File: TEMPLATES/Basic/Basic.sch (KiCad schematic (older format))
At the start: 2 parts, among them U1 CpE-3004_LP2985_LDO_1v8

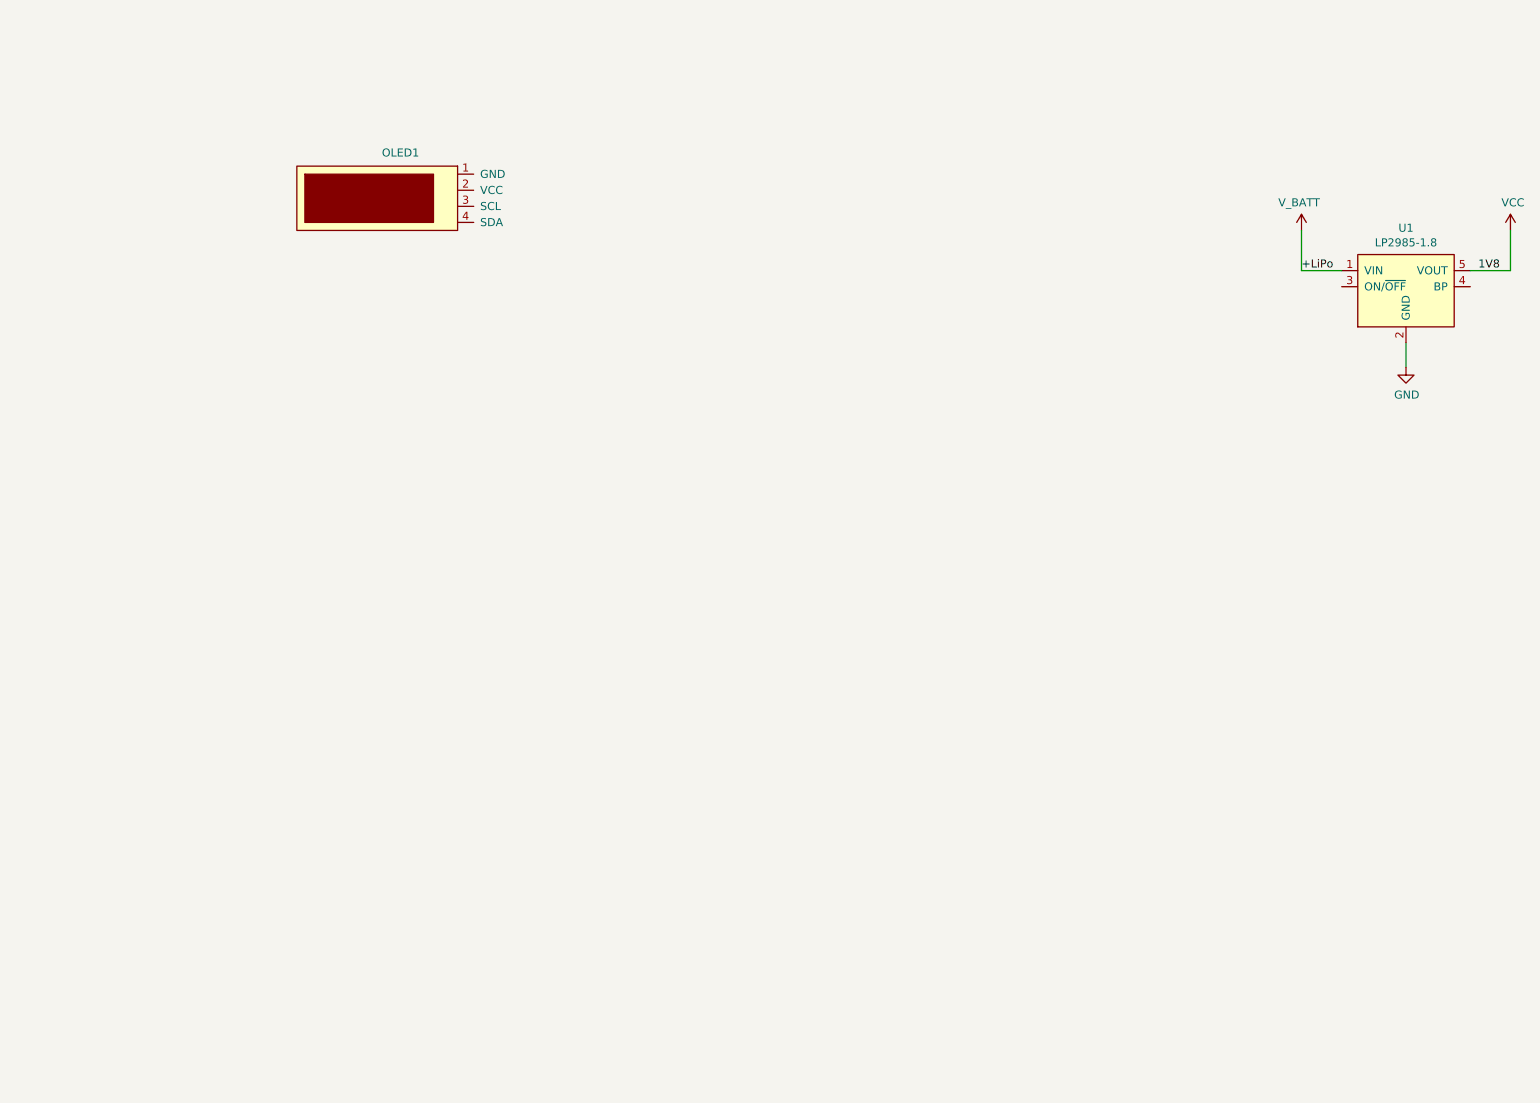
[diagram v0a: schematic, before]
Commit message: Added PCIe-x4 template
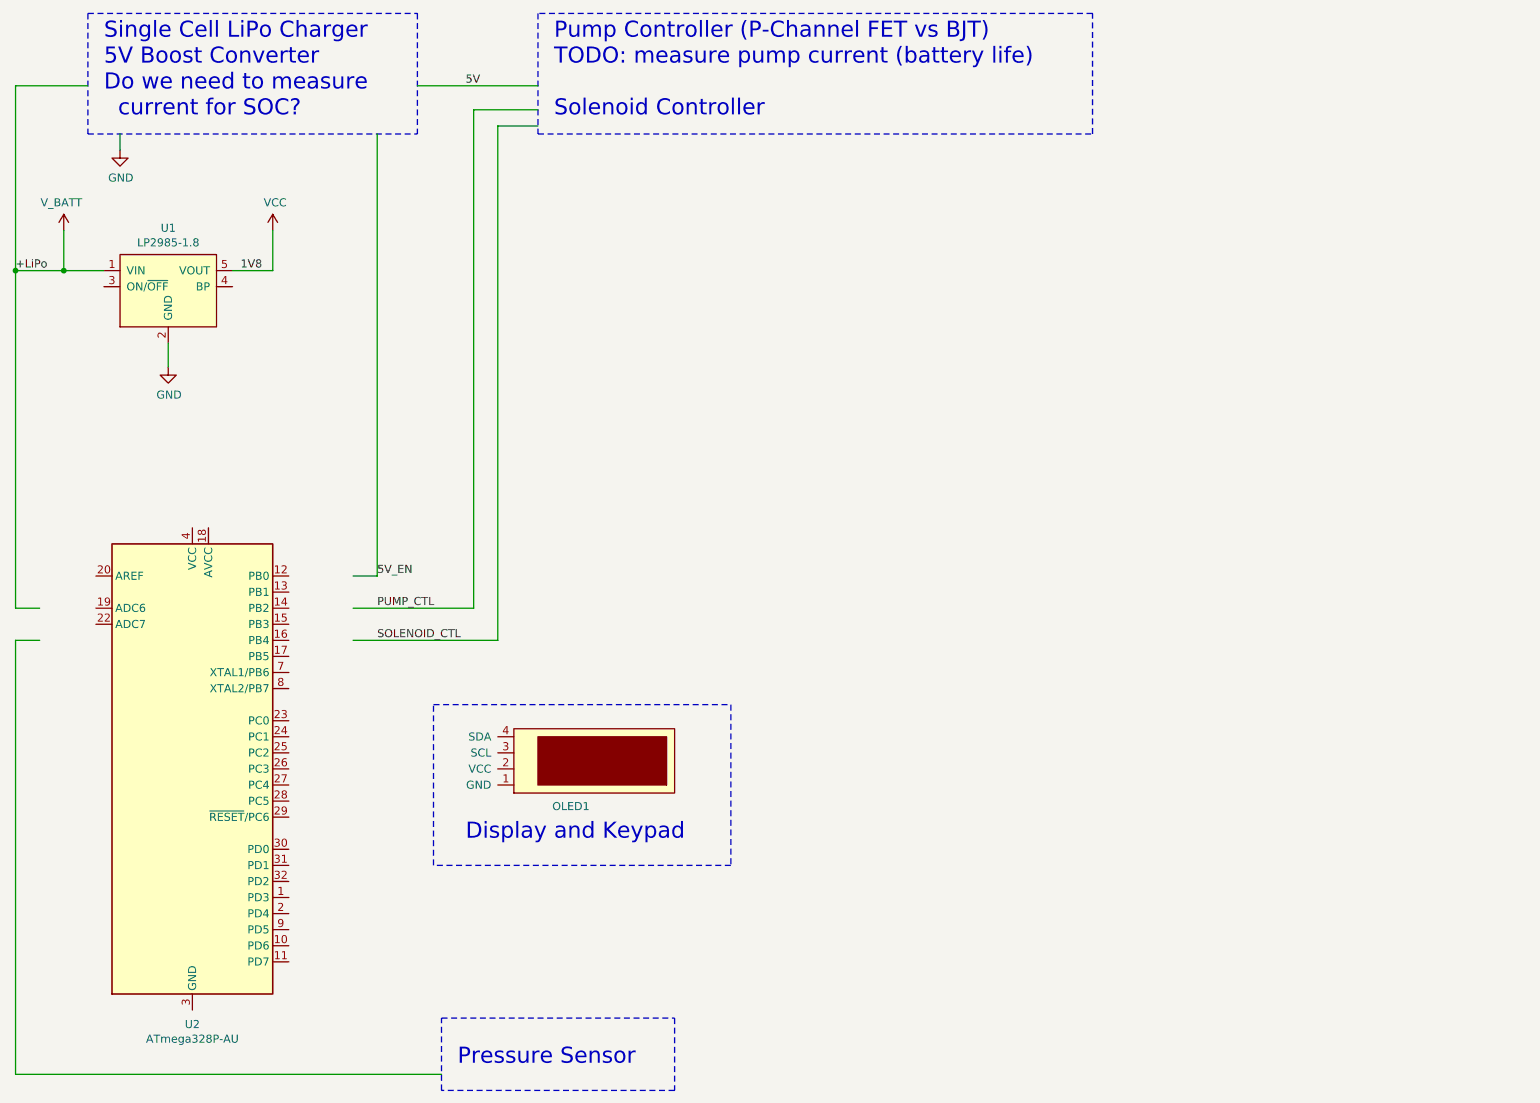
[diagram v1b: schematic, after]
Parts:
- added U2: ATmega328P-AU, Package_QFP:TQFP-32_7x7mm_P0.8mm, symbol MCU_Microchip_ATmega:ATmega328P-AU
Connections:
- net labels added: 5V, 5V_EN, PUMP_CTL, SOLENOID_CTL
- wire segments 5 -> 23
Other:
- note added: "Display and Keypad\n"
- note added: "Pressure Sensor\n"
- note added: "Pump Controller (P-Channel FET vs BJT)\nTODO: measure pump current (battery life)\n\nSolenoid Controller\n"
- note added: "Single Cell LiPo Charger\n5V Boost Converter\nDo we need to measure\n current for SOC?"
- moved on the sheet: OLED1, U1
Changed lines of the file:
@@
 EELAYER 30 0
 EELAYER END
-$Descr A4 11693 8268
+$Descr USLetter 11000 8500
 encoding utf-8
 Sheet 1 1
-Title ""
-Date ""
-Rev ""
+Title "Perfusion Pump Controller"
+Date "2021-12-02"
+Rev "0.1"
 Comp ""
 Comment1 ""
@@
 L CpE_Power:GND #PWR0101
 U 1 1 619BDDDF
-P 9550 2950
-F 0 "#PWR0101" H 9550 2700 50  0001 C CNN
-F 1 "GND" H 9555 2777 50  0000 C CNN
-F 2 "" H 9550 2950 50  0001 C CNN
-F 3 "" H 9550 2950 50  0001 C CNN
-F 4 "NA" H 9550 2950 50  0001 C CNN "CpE_PN"
-	1    9550 2950
+P 1850 2950
+F 0 "#PWR0101" H 1850 2700 50  0001 C CNN
+F 1 "GND" H 1855 2777 50  0000 C CNN
+F 2 "" H 1850 2950 50  0001 C CNN
+F 3 "" H 1850 2950 50  0001 C CNN
+F 4 "NA" H 1850 2950 50  0001 C CNN "CpE_PN"
+	1    1850 2950
 	1    0    0    -1
 $EndComp
@@
 L CpE_Integrated_Circuits:CpE-3004_LP2985_LDO_1v8 U1
 U 1 1 619BE36A
-P 9550 2450
-F 0 "U1" H 9550 2815 50  0000 C CNN
-F 1 "CpE-3004_LP2985_LDO_1v8" H 9550 2900 50  0001 C CNN
-F 2 "CpE_Integrated_Circuits:CpE-3004_LP2985_LDO_1v8" H 9550 3000 50  0001 C CNN
-F 3 "https://www.ti.com/lit/ds/symlink/lp2985.pdf?HQS=dis-dk-null-digikeymode-dsf-pf-null-wwe&ts=1637600572863" H 9550 2450 50  0001 C CNN
-F 4 "3004" H 9550 2800 50  0001 C CNN "CpE_PN"
-F 5 "LP2985-1.8" H 9550 2724 50  0000 C CNN "Val"
-	1    9550 2450
+P 1850 2450
+F 0 "U1" H 1850 2815 50  0000 C CNN
+F 1 "CpE-3004_LP2985_LDO_1v8" H 1850 2900 50  0001 C CNN
+F 2 "CpE_Integrated_Circuits:CpE-3004_LP2985_LDO_1v8" H 1850 3000 50  0001 C CNN
+F 3 "https://www.ti.com/lit/ds/symlink/lp2985.pdf?HQS=dis-dk-null-digikeymode-dsf-pf-null-wwe&ts=1637600572863" H 1850 2450 50  0001 C CNN
+F 4 "3004" H 1850 2800 50  0001 C CNN "CpE_PN"
+F 5 "LP2985-1.8" H 1850 2724 50  0000 C CNN "Val"
+	1    1850 2450
 	1    0    0    -1
 $EndComp
@@
 L CpE_Power:VCC #PWR0102
 U 1 1 619BEDF8
-P 10200 2100
-F 0 "#PWR0102" H 10200 1950 50  0001 C CNN
-F 1 "VCC" H 10215 2273 50  0000 C CNN
-F 2 "" H 10200 2100 50  0001 C CNN
-F 3 "" H 10200 2100 50  0001 C CNN
-F 4 "NA" H 10200 2100 50  0001 C CNN "CpE_PN"
-	1    10200 2100
+P 2500 2100
+F 0 "#PWR0102" H 2500 1950 50  0001 C CNN
+F 1 "VCC" H 2515 2273 50  0000 C CNN
+F 2 "" H 2500 2100 50  0001 C CNN
+F 3 "" H 2500 2100 50  0001 C CNN
+F 4 "NA" H 2500 2100 50  0001 C CNN "CpE_PN"
+	1    2500 2100
 	1    0    0    -1
 $EndComp
-Text Label 10000 2350 0    50   ~ 0
+Text Label 2300 2350 0    50   ~ 0
 1V8
 Wire Wire Line
-	9950 2350 10200 2350
+	2250 2350 2500 2350
 Wire Wire Line
-	10200 2350 10200 2100
+	2500 2350 2500 2100
 Wire Wire Line
-	9550 2950 9550 2800
+	1850 2950 1850 2800
 $Comp
 L CpE_Power:V_BATT #PWR1
 U 1 1 619C0899
-P 8900 2100
-F 0 "#PWR1" H 8900 2100 50  0001 C CNN
-F 1 "V_BATT" H 8885 2273 50  0000 C CNN
-F 2 "" H 8900 2100 50  0001 C CNN
-F 3 "" H 8900 2100 50  0001 C CNN
-	1    8900 2100
+P 1200 2100
+F 0 "#PWR1" H 1200 2100 50  0001 C CNN
+F 1 "V_BATT" H 1185 2273 50  0000 C CNN
+F 2 "" H 1200 2100 50  0001 C CNN
+F 3 "" H 1200 2100 50  0001 C CNN
+	1    1200 2100
 	1    0    0    -1
 $EndComp
 Wire Wire Line
-	8900 2100 8900 2350
+	1200 2100 1200 2350
 Wire Wire Line
-	8900 2350 9150 2350
-Text Label 8900 2350 0    50   ~ 0
+	1200 2350 1450 2350
+Text Label 900  2350 0    50   ~ 0
 +LiPo
 $Comp
 L CpE_Opto_Electronics:CpE-3005_OLED_I2C_128x32 OLED1
 U 1 1 619C1A31
-P 3150 1900
-F 0 "OLED1" H 3295 2183 50  0000 C CNN
-F 1 "CpE-3005_OLED_I2C_128x32" H 3150 2250 50  0001 C CNN
-F 2 "CpE_Opto_Electronics:3005_OLED_I2C_128x32" H 3150 1900 50  0001 C CNN
-F 3 "https://www.amazon.com/Pieces-Display-Module-SSD1306-3-3V-5V/dp/B08L7QW7SR/ref=sr_1_1?keywords=B08L7QW7SR&qid=1637605536&sr=8-1" H 3150 1900 50  0001 C CNN
-F 4 "3005" H 3150 2150 50  0001 C CNN "CpE_PN"
-F 5 "" H 3150 1900 50  0000 C CNN "Val"
-	1    3150 1900
+P 4500 5400
+F 0 "OLED1" H 4645 5683 50  0000 C CNN
+F 1 "CpE-3005_OLED_I2C_128x32" H 4500 5750 50  0001 C CNN
+F 2 "CpE_Opto_Electronics:3005_OLED_I2C_128x32" H 4500 5400 50  0001 C CNN
+F 3 "https://www.amazon.com/Pieces-Display-Module-SSD1306-3-3V-5V/dp/B08L7QW7SR/ref=sr_1_1?keywords=B08L7QW7SR&qid=1637605536&sr=8-1" H 4500 5400 50  0001 C CNN
+F 4 "3005" H 4500 5650 50  0001 C CNN "CpE_PN"
+F 5 "" H 4500 5400 50  0000 C CNN "Val"
+	1    4500 5400
+	-1   0    0    1
+$EndComp
+$Comp
+L MCU_Microchip_ATmega:ATmega328P-AU U2
+U 1 1 61A9199E
+P 2000 5450
+F 0 "U2" H 2000 3861 50  0000 C CNN
+F 1 "ATmega328P-AU" H 2000 3770 50  0000 C CNN
+F 2 "Package_QFP:TQFP-32_7x7mm_P0.8mm" H 2000 5450 50  0001 C CIN
+F 3 "http://ww1.microchip.com/downloads/en/DeviceDoc/ATmega328_P%20AVR%20MCU%20with%20picoPower%20Technology%20Data%20Sheet%2040001984A.pdf" H 2000 5450 50  0001 C CNN
+	1    2000 5450
 	1    0    0    -1
 $EndComp
+Text Notes 1450 1400 0    100  ~ 0
+Single Cell LiPo Charger\n5V Boost Converter\nDo we need to measure\n  current for SOC?
+Wire Wire Line
+	1200 2350 900  2350
+Wire Wire Line
+	900  2350 900  1200
+Wire Wire Line
+	900  1200 1350 1200
+Connection ~ 1200 2350
+Wire Notes Line
+	1350 1500 3400 1500
+$Comp
+L CpE_Power:GND #PWR?
+U 1 1 61A9943F
+P 1550 1600
+F 0 "#PWR?" H 1550 1350 50  0001 C CNN
+F 1 "GND" H 1555 1427 50  0000 C CNN
+F 2 "" H 1550 1600 50  0001 C CNN
+F 3 "" H 1550 1600 50  0001 C CNN
+F 4 "NA" H 1550 1600 50  0001 C CNN "CpE_PN"
+	1    1550 1600
+	1    0    0    -1
+$EndComp
+Wire Wire Line
+	1550 1600 1550 1500
+Wire Wire Line
+	3150 1500 3150 4250
+Wire Wire Line
+	3150 4250 3000 4250
+Text Label 3150 4250 0    50   ~ 0
+5V_EN
+Wire Wire Line
+	3400 1200 4150 1200
+Text Label 3700 1200 0    50   ~ 0
+5V
+Text Notes 4250 1400 0    100  ~ 0
+Pump Controller (P-Channel FET vs BJT)\nTODO: measure pump current (battery life)\n\nSolenoid Controller\n
+Wire Wire Line
+	900  2350 900  4450
+Wire Wire Line
+	900  4450 1050 4450
+Connection ~ 900  2350
+Wire Notes Line
+	1350 750  3400 750
+Wire Notes Line
+	1350 750  1350 1500
+Wire Notes Line
+	3400 750  3400 1500
+Text Notes 3650 7300 0    100  ~ 0
+Pressure Sensor\n
+Text Notes 3700 5900 0    100  ~ 0
+Display and Keypad\n
+Wire Notes Line
+	4150 750  4150 1500
+Wire Notes Line
+	4150 1500 7600 1500
+Wire Notes Line
+	7600 1500 7600 750
+Wire Notes Line
+	7600 750  4150 750
+Wire Wire Line
+	3750 1350 3750 4450
+Wire Wire Line
+	3750 4450 3000 4450
+Wire Wire Line
+	3750 1350 4150 1350
+Wire Wire Line
+	4150 1450 3900 1450
+Wire Wire Line
+	3900 1450 3900 4650
+Wire Wire Line
+	3900 4650 3000 4650
+Text Label 3150 4450 0    50   ~ 0
+PUMP_CTL
+Text Label 3150 4650 0    50   ~ 0
+SOLENOID_CTL
+Wire Notes Line
+	3500 5050 5350 5050
+Wire Notes Line
+	5350 5050 5350 6050
+Wire Notes Line
+	5350 6050 3500 6050
+Wire Notes Line
+	3500 6050 3500 5050
+Wire Notes Line
+	3550 7000 5000 7000
+Wire Notes Line
+	5000 7000 5000 7450
+Wire Notes Line
+	5000 7450 3550 7450
+Wire Notes Line
+	3550 7450 3550 7000
+Wire Wire Line
+	3550 7350 900  7350
+Wire Wire Line
+	900  7350 900  4650
+Wire Wire Line
+	900  4650 1050 4650
 $EndSCHEMATC
